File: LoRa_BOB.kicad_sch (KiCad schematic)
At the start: 8 parts, among them U1 1597-1488-ND, U2 XC6210B332MR-G, U3 74HC4050D

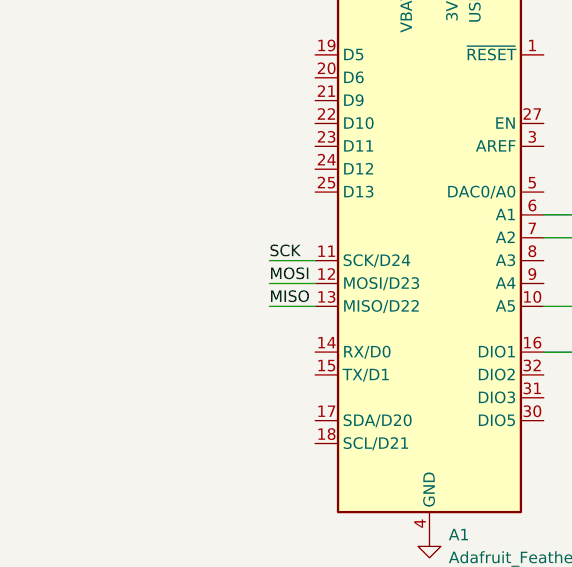
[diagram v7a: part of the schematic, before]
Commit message: netclass routing
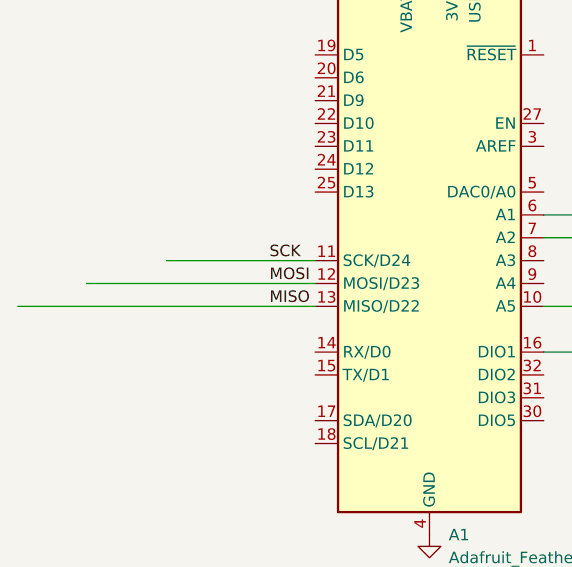
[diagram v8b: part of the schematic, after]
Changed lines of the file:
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@@
+	(wire
+		(pts
+			(xy 125.73 129.54) (xy 158.75 129.54)
+		)
+		(stroke
+			(width 0)
+			(type default)
+		)
+	)
 	(wire
 		(pts
@@
 	(wire
 		(pts
-			(xy 153.67 124.46) (xy 158.75 124.46)
-		)
-		(stroke
-			(width 0)
-			(type default)
-		)
-	)
-	(wire
-		(pts
 			(xy 292.1 114.3) (xy 302.26 114.3)
 		)
@@
 	(wire
 		(pts
+			(xy 133.35 127) (xy 158.75 127)
+		)
+		(stroke
+			(width 0)
+			(type default)
+		)
+	)
+	(wire
+		(pts
 			(xy 232.41 88.9) (xy 232.41 90.17)
 		)
@@
 	(wire
 		(pts
-			(xy 153.67 129.54) (xy 158.75 129.54)
-		)
-		(stroke
-			(width 0)
-			(type default)
-		)
-	)
-	(wire
-		(pts
 			(xy 203.2 129.54) (xy 210.82 129.54)
 		)
@@
 	(wire
 		(pts
-			(xy 153.67 127) (xy 158.75 127)
-		)
-		(stroke
-			(width 0)
-			(type default)
-		)
-	)
-	(wire
-		(pts
 			(xy 184.15 121.92) (xy 210.82 121.92)
 		)
@@
 		(pts
 			(xy 236.22 121.92) (xy 266.7 121.92)
+		)
+		(stroke
+			(width 0)
+			(type default)
+		)
+	)
+	(wire
+		(pts
+			(xy 142.24 124.46) (xy 158.75 124.46)
 		)
 		(stroke
@@
 		)
 	)
+	(netclass_flag ""
+		(length 2.54)
+		(shape round)
+		(at 142.24 124.46 0)
+		(fields_autoplaced yes)
+		(effects
+			(font
+				(size 1.27 1.27)
+			)
+			(justify left bottom)
+		)
+		(property "Netclass" "50 ohm"
+			(at 142.9385 121.92 0)
+			(effects
+				(font
+					(size 1.27 1.27)
+				)
+				(justify left)
+			)
+		)
+		(property "Component Class" ""
+			(at -1.27 1.27 0)
+			(effects
+				(font
+					(size 1.27 1.27)
+					(italic yes)
+				)
+			)
+		)
+	)
+	(netclass_flag ""
+		(length 2.54)
+		(shape round)
+		(at 133.35 127 0)
+		(fields_autoplaced yes)
+		(effects
+			(font
+				(size 1.27 1.27)
+			)
+			(justify left bottom)
+		)
+		(property "Netclass" "50 ohm"
+			(at 134.0485 124.46 0)
+			(effects
+				(font
+					(size 1.27 1.27)
+				)
+				(justify left)
+			)
+		)
+		(property "Component Class" ""
+			(at -20.32 0 0)
+			(effects
+				(font
+					(size 1.27 1.27)
+					(italic yes)
+				)
+			)
+		)
+	)
+	(netclass_flag ""
+		(length 2.54)
+		(shape round)
+		(at 295.91 114.3 0)
+		(fields_autoplaced yes)
+		(effects
+			(font
+				(size 1.27 1.27)
+			)
+			(justify left bottom)
+		)
+		(property "Netclass" "50 ohm"
+			(at 296.6085 111.76 0)
+			(effects
+				(font
+					(size 1.27 1.27)
+				)
+				(justify left)
+			)
+		)
+		(property "Component Class" ""
+			(at -200.66 -34.29 0)
+			(effects
+				(font
+					(size 1.27 1.27)
+					(italic yes)
+				)
+			)
+		)
+	)
+	(netclass_flag ""
+		(length 2.54)
+		(shape round)
+		(at 254 114.3 0)
+		(fields_autoplaced yes)
+		(effects
+			(font
+				(size 1.27 1.27)
+			)
+			(justify left bottom)
+		)
+		(property "Netclass" "50 ohm"
+			(at 254.6985 111.76 0)
+			(effects
+				(font
+					(size 1.27 1.27)
+				)
+				(justify left)
+			)
+		)
+		(property "Component Class" ""
+			(at 0 -10.16 0)
+			(effects
+				(font
+					(size 1.27 1.27)
+					(italic yes)
+				)
+			)
+		)
+	)
+	(netclass_flag ""
+		(length 2.54)
+		(shape round)
+		(at 125.73 129.54 0)
+		(fields_autoplaced yes)
+		(effects
+			(font
+				(size 1.27 1.27)
+			)
+			(justify left bottom)
+		)
+		(property "Netclass" "50 ohm"
+			(at 126.4285 127 0)
+			(effects
+				(font
+					(size 1.27 1.27)
+				)
+				(justify left)
+			)
+		)
+		(property "Component Class" ""
+			(at -19.05 1.27 0)
+			(effects
+				(font
+					(size 1.27 1.27)
+					(italic yes)
+				)
+			)
+		)
+	)
+	(netclass_flag ""
+		(length 2.54)
+		(shape round)
+		(at 256.54 119.38 0)
+		(fields_autoplaced yes)
+		(effects
+			(font
+				(size 1.27 1.27)
+			)
+			(justify left bottom)
+		)
+		(property "Netclass" "50 ohm"
+			(at 257.2385 116.84 0)
+			(effects
+				(font
+					(size 1.27 1.27)
+				)
+				(justify left)
+			)
+		)
+		(property "Component Class" ""
+			(at 2.54 -5.08 0)
+			(effects
+				(font
+					(size 1.27 1.27)
+					(italic yes)
+				)
+			)
+		)
+	)
+	(netclass_flag ""
+		(length 2.54)
+		(shape round)
+		(at 246.38 129.54 0)
+		(fields_autoplaced yes)
+		(effects
+			(font
+				(size 1.27 1.27)
+			)
+			(justify left bottom)
+		)
+		(property "Netclass" "50 ohm"
+			(at 247.0785 127 0)
+			(effects
+				(font
+					(size 1.27 1.27)
+				)
+				(justify left)
+			)
+		)
+		(property "Component Class" ""
+			(at -1.27 0 0)
+			(effects
+				(font
+					(size 1.27 1.27)
+					(italic yes)
+				)
+			)
+		)
+	)
